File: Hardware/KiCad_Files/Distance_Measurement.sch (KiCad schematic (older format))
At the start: 8 parts, among them J1 Conn_01x04_Female, J2 Screw_Terminal_01x02, Q1 2N5109, U1 WeMos_D1_mini

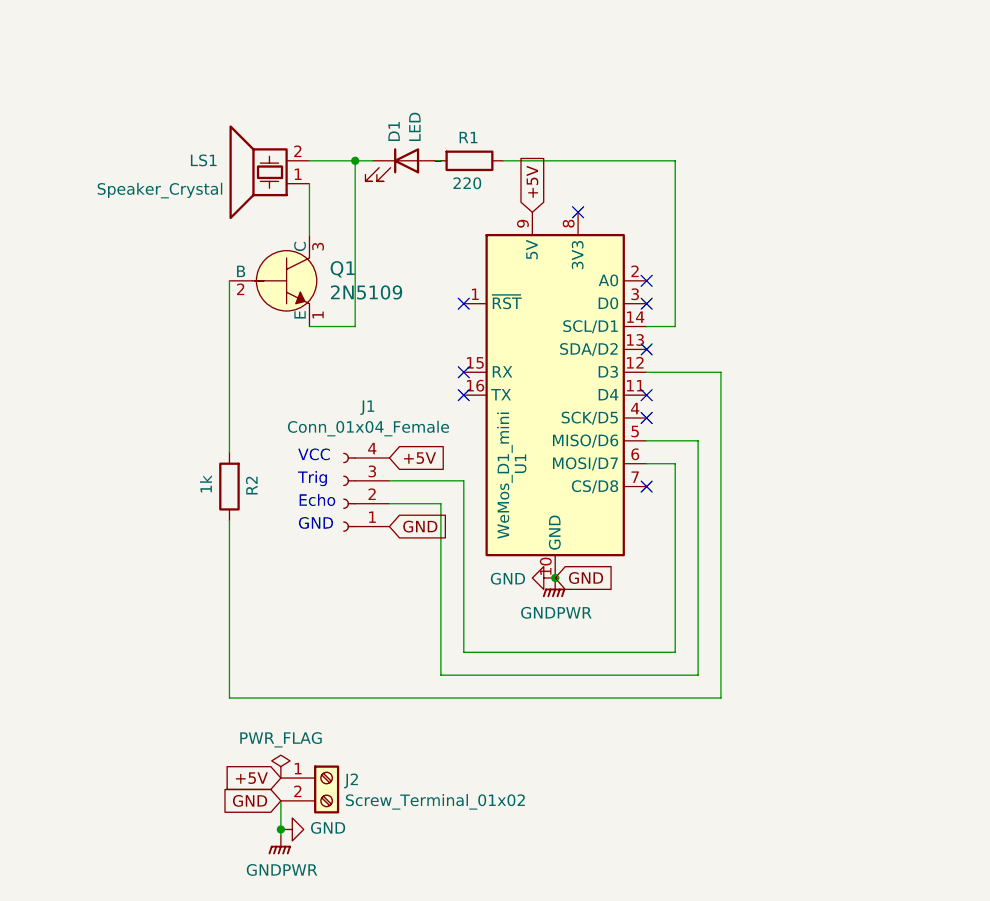
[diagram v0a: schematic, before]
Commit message: corrected failure on PCB
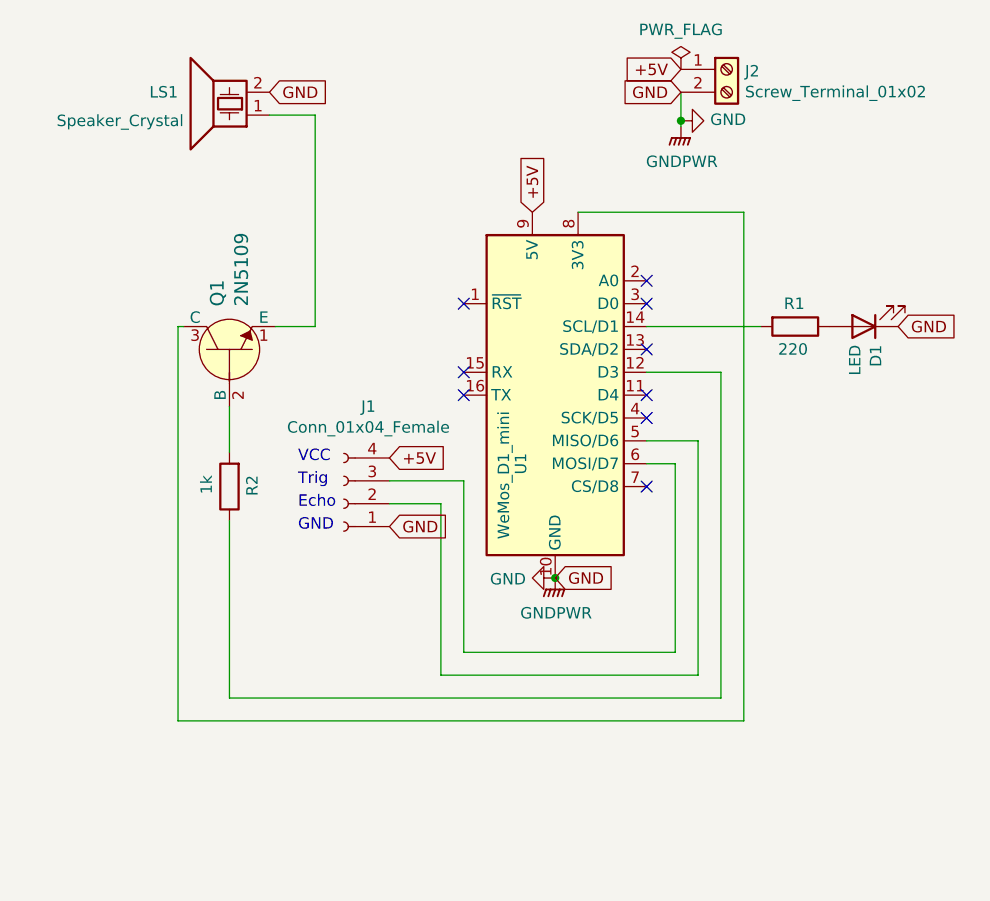
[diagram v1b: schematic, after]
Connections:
- net GND: now also D1.1 (K), LS1.2
- net at U1.14 (SCL/D1): now also R1.2; no longer R1.1
- net at U1.8 (3V3): now also Q1.3 (C)
- net at D1.2 (A): now also R1.1; no longer R1.2
- net at LS1.1: now also Q1.1 (E); no longer Q1.3 (C)
- no-connect marks 10 -> 9
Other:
- moved on the sheet: D1, J2, LS1, Q1, R1
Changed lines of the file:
@@
 Sheet 1 1
 Title "WemosD1 mini Distance Measurement"
-Date "2021-10-17"
-Rev "Rev. 00"
+Date "2021-11-11"
+Rev "Rev. 02"
 Comp "Emilia & Papa"
 Comment1 ""
@@
 L Device:LED D1
 U 1 1 616C95CA
-P 5100 2375
-F 0 "D1" V 5047 2455 50  0000 L CNN
-F 1 "LED" V 5138 2455 50  0000 L CNN
-F 2 "LED_THT:LED_D3.0mm" H 5100 2375 50  0001 C CNN
-F 3 "~" H 5100 2375 50  0001 C CNN
-	1    5100 2375
-	1    0    0    -1
+P 7100 3100
+F 0 "D1" V 7047 3180 50  0000 L CNN
+F 1 "LED" V 7138 3180 50  0000 L CNN
+F 2 "LED_THT:LED_D3.0mm" H 7100 3100 50  0001 C CNN
+F 3 "~" H 7100 3100 50  0001 C CNN
+	1    7100 3100
+	-1   0    0    1
 $EndComp
 $Comp
@@
 L Device:R R1
 U 1 1 616CA772
-P 5375 2375
-F 0 "R1" V 5275 2325 50  0000 L CNN
-F 1 "220" V 5475 2300 50  0000 L CNN
-F 2 "Resistor_THT:R_Axial_DIN0207_L6.3mm_D2.5mm_P10.16mm_Horizontal" V 5305 2375 50  0001 C CNN
-F 3 "~" H 5375 2375 50  0001 C CNN
-	1    5375 2375
+P 6800 3100
+F 0 "R1" V 6700 3050 50  0000 L CNN
+F 1 "220" V 6900 3025 50  0000 L CNN
+F 2 "Resistor_THT:R_Axial_DIN0207_L6.3mm_D2.5mm_P10.16mm_Horizontal" V 6730 3100 50  0001 C CNN
+F 3 "~" H 6800 3100 50  0001 C CNN
+	1    6800 3100
 	0    1    1    0
 $EndComp
@@
 L Device:Speaker_Crystal LS1
 U 1 1 616CE39B
-P 4475 2475
-F 0 "LS1" H 4675 2375 50  0000 L CNN
-F 1 "Speaker_Crystal" H 4650 2500 50  0000 L CNN
-F 2 "digikey-footprints:Piezo_Transducer_THT_PS1240P02BT" H 4440 2425 50  0001 C CNN
-F 3 "~" H 4440 2425 50  0001 C CNN
-	1    4475 2475
+P 4300 2175
+F 0 "LS1" H 4500 2075 50  0000 L CNN
+F 1 "Speaker_Crystal" H 4475 2200 50  0000 L CNN
+F 2 "digikey-footprints:Piezo_Transducer_THT_PS1240P02BT" H 4265 2125 50  0001 C CNN
+F 3 "~" H 4265 2125 50  0001 C CNN
+	1    4300 2175
 	-1   0    0    1
 $EndComp
@@
 L Connector:Screw_Terminal_01x02 J2
 U 1 1 616C480C
-P 4750 5075
-F 0 "J2" H 4830 5067 50  0000 L CNN
-F 1 "Screw_Terminal_01x02" H 4830 4976 50  0000 L CNN
-F 2 "TerminalBlock_Phoenix:TerminalBlock_Phoenix_MPT-0,5-2-2.54_1x02_P2.54mm_Horizontal" H 4750 5075 50  0001 C CNN
-F 3 "~" H 4750 5075 50  0001 C CNN
-	1    4750 5075
-	1    0    0    -1
-$EndComp
-Text GLabel 4550 5075 0    50   Input ~ 0
+P 6500 1975
+F 0 "J2" H 6580 1967 50  0000 L CNN
+F 1 "Screw_Terminal_01x02" H 6580 1876 50  0000 L CNN
+F 2 "TerminalBlock_Phoenix:TerminalBlock_Phoenix_MPT-0,5-2-2.54_1x02_P2.54mm_Horizontal" H 6500 1975 50  0001 C CNN
+F 3 "~" H 6500 1975 50  0001 C CNN
+	1    6500 1975
+	1    0    0    -1
+$EndComp
+Text GLabel 6300 1975 0    50   Input ~ 0
 +5V
-Text GLabel 4550 5175 0    50   Input ~ 0
+Text GLabel 6300 2075 0    50   Input ~ 0
 GND
 $Comp
 L power:PWR_FLAG #FLG01
 U 1 1 616CBB59
-P 4550 5075
-F 0 "#FLG01" H 4550 5150 50  0001 C CNN
-F 1 "PWR_FLAG" H 4550 5248 50  0000 C CNN
-F 2 "" H 4550 5075 50  0001 C CNN
-F 3 "~" H 4550 5075 50  0001 C CNN
-	1    4550 5075
+P 6300 1975
+F 0 "#FLG01" H 6300 2050 50  0001 C CNN
+F 1 "PWR_FLAG" H 6300 2148 50  0000 C CNN
+F 2 "" H 6300 1975 50  0001 C CNN
+F 3 "~" H 6300 1975 50  0001 C CNN
+	1    6300 1975
 	1    0    0    -1
 $EndComp
 Text GLabel 5650 2600 1    50   Input ~ 0
 +5V
-NoConn ~ 5850 2600
 NoConn ~ 5350 3000
 NoConn ~ 5350 3300
@@
 Wire Wire Line
 	6150 3600 6375 3600
-Wire Wire Line
-	6150 3100 6275 3100
-Wire Wire Line
-	6275 3100 6275 2375
-Wire Wire Line
-	6275 2375 5525 2375
-Wire Wire Line
-	5250 2375 5225 2375
 $Comp
 L Connector:Conn_01x04_Female J1
@@
 	-1   0    0    1
 $EndComp
-$Comp
-L dk_Transistors-Bipolar-BJT-RF:2N5109 Q1
-U 1 1 616E3576
-P 4675 2900
-F 0 "Q1" H 4763 2953 60  0000 L CNN
-F 1 "2N5109" H 4763 2847 60  0000 L CNN
-F 2 "Package_TO_SOT_THT:TO-92_Inline_Wide" H 4875 3100 60  0001 L CNN
-F 3 "https://my.centralsemi.com/get_document.php?cmp=1&mergetype=pd&mergepath=pd&pdf_id=2N5109.PDF" H 4875 3200 60  0001 L CNN
-F 4 "2N5109CS-ND" H 4875 3300 60  0001 L CNN "Digi-Key_PN"
-F 5 "2N5109" H 4875 3400 60  0001 L CNN "MPN"
-F 6 "Discrete Semiconductor Products" H 4875 3500 60  0001 L CNN "Category"
-F 7 "Transistors - Bipolar (BJT) - RF" H 4875 3600 60  0001 L CNN "Family"
-F 8 "https://my.centralsemi.com/get_document.php?cmp=1&mergetype=pd&mergepath=pd&pdf_id=2N5109.PDF" H 4875 3700 60  0001 L CNN "DK_Datasheet_Link"
-F 9 "/product-detail/en/central-semiconductor-corp/2N5109/2N5109CS-ND/4806909" H 4875 3800 60  0001 L CNN "DK_Detail_Page"
-F 10 "RF TRANS NPN 20V 1.2GHZ TO39" H 4875 3900 60  0001 L CNN "Description"
-F 11 "Central Semiconductor Corp" H 4875 4000 60  0001 L CNN "Manufacturer"
-F 12 "Active" H 4875 4100 60  0001 L CNN "Status"
-	1    4675 2900
-	1    0    0    -1
-$EndComp
-Wire Wire Line
-	4950 2375 4875 2375
-Wire Wire Line
-	4875 2375 4875 3100
-Wire Wire Line
-	4875 3100 4675 3100
 Wire Wire Line
 	6475 4725 6475 3300
@@
 	6475 3300 6150 3300
 Wire Wire Line
-	4325 3650 4325 2900
+	4325 3650 4325 3450
 Wire Wire Line
 	4325 3950 4325 4725
 Wire Wire Line
 	4325 4725 6475 4725
-Connection ~ 4875 2375
-Wire Wire Line
-	4675 2375 4875 2375
-Wire Wire Line
-	4675 2700 4675 2475
 $Comp
 L power:GNDPWR #PWR0101
 U 1 1 616FD5B6
-P 4550 5325
-F 0 "#PWR0101" H 4550 5125 50  0001 C CNN
-F 1 "GNDPWR" H 4554 5171 50  0000 C CNN
-F 2 "" H 4550 5275 50  0001 C CNN
-F 3 "" H 4550 5275 50  0001 C CNN
-	1    4550 5325
-	1    0    0    -1
-$EndComp
-Wire Wire Line
-	4550 5325 4550 5300
+P 6300 2225
+F 0 "#PWR0101" H 6300 2025 50  0001 C CNN
+F 1 "GNDPWR" H 6304 2071 50  0000 C CNN
+F 2 "" H 6300 2175 50  0001 C CNN
+F 3 "" H 6300 2175 50  0001 C CNN
+	1    6300 2225
+	1    0    0    -1
+$EndComp
+Wire Wire Line
+	6300 2225 6300 2200
 $Comp
 L power:GND #PWR0102
 U 1 1 616FF170
-P 4550 5300
-F 0 "#PWR0102" H 4550 5050 50  0001 C CNN
-F 1 "GND" V 4555 5172 50  0000 R CNN
-F 2 "" H 4550 5300 50  0001 C CNN
-F 3 "" H 4550 5300 50  0001 C CNN
-	1    4550 5300
+P 6300 2200
+F 0 "#PWR0102" H 6300 1950 50  0001 C CNN
+F 1 "GND" V 6305 2072 50  0000 R CNN
+F 2 "" H 6300 2200 50  0001 C CNN
+F 3 "" H 6300 2200 50  0001 C CNN
+	1    6300 2200
 	0    -1   -1   0
 $EndComp
-Connection ~ 4550 5300
-Wire Wire Line
-	4550 5300 4550 5175
+Connection ~ 6300 2200
+Wire Wire Line
+	6300 2200 6300 2075
 $Comp
 L power:GND #PWR0103
@@
 $EndComp
 Connection ~ 5750 4200
+Text GLabel 7250 3100 2    50   Input ~ 0
+GND
+Wire Wire Line
+	5850 2600 6575 2600
+Wire Wire Line
+	6575 2600 6575 4825
+Wire Wire Line
+	6575 4825 4100 4825
+Wire Wire Line
+	4100 4825 4100 3100
+Wire Wire Line
+	4500 2175 4700 2175
+Text GLabel 4500 2075 2    50   Input ~ 0
+GND
+$Comp
+L dk_Transistors-Bipolar-BJT-RF:2N5109 Q1
+U 1 1 616E3576
+P 4325 3100
+F 0 "Q1" H 4413 3153 60  0000 L CNN
+F 1 "2N5109" H 4413 3047 60  0000 L CNN
+F 2 "Package_TO_SOT_THT:TO-92_Inline_Wide" H 4525 3300 60  0001 L CNN
+F 3 "https://my.centralsemi.com/get_document.php?cmp=1&mergetype=pd&mergepath=pd&pdf_id=2N5109.PDF" H 4525 3400 60  0001 L CNN
+F 4 "2N5109CS-ND" H 4525 3500 60  0001 L CNN "Digi-Key_PN"
+F 5 "2N5109" H 4525 3600 60  0001 L CNN "MPN"
+F 6 "Discrete Semiconductor Products" H 4525 3700 60  0001 L CNN "Category"
+F 7 "Transistors - Bipolar (BJT) - RF" H 4525 3800 60  0001 L CNN "Family"
+F 8 "https://my.centralsemi.com/get_document.php?cmp=1&mergetype=pd&mergepath=pd&pdf_id=2N5109.PDF" H 4525 3900 60  0001 L CNN "DK_Datasheet_Link"
+F 9 "/product-detail/en/central-semiconductor-corp/2N5109/2N5109CS-ND/4806909" H 4525 4000 60  0001 L CNN "DK_Detail_Page"
+F 10 "RF TRANS NPN 20V 1.2GHZ TO39" H 4525 4100 60  0001 L CNN "Description"
+F 11 "Central Semiconductor Corp" H 4525 4200 60  0001 L CNN "Manufacturer"
+F 12 "Active" H 4525 4300 60  0001 L CNN "Status"
+	1    4325 3100
+	0    -1   -1   0
+$EndComp
+Wire Wire Line
+	4700 2175 4700 3100
+Wire Wire Line
+	4125 3100 4100 3100
+Wire Wire Line
+	4525 3100 4700 3100
+Wire Wire Line
+	6650 3100 6150 3100
 $EndSCHEMATC
